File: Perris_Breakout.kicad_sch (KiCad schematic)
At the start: 21 parts, among them J1 PERRI_1, J10 SCL, J11 GND, J12 GND, J13 SDA, J14 SDA, J2 PERRI_2, J3 PERRI_3, J4 PERRI_4, J5 PERRI_5, J6 PERRI_6, J7 PERRI_7, J8 PERRI_8, J9 SCL

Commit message: Changed copper zone properties
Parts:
- J1, J2, J3, J4, J5, J6, J7, J8: footprint Connector_PinHeader_2.54mm:PinHeader_2x05_P2.54mm_Vertical -> HELIX:Perri_conn_2x5_Reverse
- J10, J9, TP1: value SCL -> SDA
- J13, J14, TP3: value SDA -> SCL
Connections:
- net SCL: now also J13.1 (Pin_1), J14.1 (Pin_1), TP3.1; no longer J10.1 (Pin_1), J9.1 (Pin_1), TP1.1
- net SDA: now also J10.1 (Pin_1), J9.1 (Pin_1), TP1.1; no longer J13.1 (Pin_1), J14.1 (Pin_1), TP3.1
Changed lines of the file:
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@@
+    (effects (font (size 1.27 1.27)) (justify left bottom))
+  )
+  (label "SDA" (at 199.39 93.98 0)
     (effects (font (size 1.27 1.27)) (justify left bottom))
   )
@@
     (effects (font (size 1.27 1.27)) (justify left bottom))
   )
-  (label "SDA" (at 199.39 124.46 90)
-    (effects (font (size 1.27 1.27)) (justify left bottom))
-  )
   (label "SCL" (at 101.6 54.61 180)
     (effects (font (size 1.27 1.27)) (justify right bottom))
   )
-  (label "SCL" (at 199.39 93.98 90)
-    (effects (font (size 1.27 1.27)) (justify left bottom))
-  )
   (label "SDA" (at 114.3 54.61 0)
     (effects (font (size 1.27 1.27)) (justify left bottom))
@@
   )
   (label "GND" (at 213.36 64.77 0)
+    (effects (font (size 1.27 1.27)) (justify left bottom))
+  )
+  (label "SCL" (at 199.39 124.46 0)
     (effects (font (size 1.27 1.27)) (justify left bottom))
   )
@@
       (effects (font (size 1.27 1.27)) (justify left))
     )
-    (property "Value" "SCL" (id 1) (at 180.34 83.82 90)
+    (property "Value" "SDA" (id 1) (at 180.34 83.82 90)
       (effects (font (size 1.27 1.27)) (justify left))
     )
@@
     (property "Reference" "J1" (id 0) (at 77.47 19.05 0))
     (property "Value" "PERRI_1" (id 1) (at 77.47 21.59 0))
-    (property "Footprint" "Connector_PinHeader_2.54mm:PinHeader_2x05_P2.54mm_Vertical" (id 2) (at 76.2 30.48 0)
+    (property "Footprint" "HELIX:Perri_conn_2x5_Reverse" (id 2) (at 76.2 30.48 0)
       (effects (font (size 1.27 1.27)) hide)
     )
@@
       (effects (font (size 1.27 1.27)) (justify left))
     )
-    (property "Value" "SCL" (id 1) (at 200.66 88.8999 0)
+    (property "Value" "SDA" (id 1) (at 200.66 88.8999 0)
       (effects (font (size 1.27 1.27)) (justify left))
     )
@@
     (property "Reference" "J3" (id 0) (at 73.66 97.79 0))
     (property "Value" "PERRI_3" (id 1) (at 73.66 100.33 0))
-    (property "Footprint" "Connector_PinHeader_2.54mm:PinHeader_2x05_P2.54mm_Vertical" (id 2) (at 72.39 109.22 0)
+    (property "Footprint" "HELIX:Perri_conn_2x5_Reverse" (id 2) (at 72.39 109.22 0)
       (effects (font (size 1.27 1.27)) hide)
     )
@@
     (property "Reference" "J4" (id 0) (at 73.66 138.43 0))
     (property "Value" "PERRI_4" (id 1) (at 73.66 140.97 0))
-    (property "Footprint" "Connector_PinHeader_2.54mm:PinHeader_2x05_P2.54mm_Vertical" (id 2) (at 72.39 149.86 0)
+    (property "Footprint" "HELIX:Perri_conn_2x5_Reverse" (id 2) (at 72.39 149.86 0)
       (effects (font (size 1.27 1.27)) hide)
     )
@@
       (effects (font (size 1.27 1.27)) (justify left))
     )
-    (property "Value" "SDA" (id 1) (at 220.98 113.6649 90)
+    (property "Value" "SCL" (id 1) (at 220.98 113.6649 90)
       (effects (font (size 1.27 1.27)) (justify left))
     )
@@
       (effects (font (size 1.27 1.27)) (justify left))
     )
-    (property "Value" "SDA" (id 1) (at 200.66 118.1099 0)
+    (property "Value" "SCL" (id 1) (at 200.66 118.1099 0)
       (effects (font (size 1.27 1.27)) (justify left))
     )
@@
     (property "Reference" "J2" (id 0) (at 73.66 57.15 0))
     (property "Value" "PERRI_2" (id 1) (at 73.66 59.69 0))
-    (property "Footprint" "Connector_PinHeader_2.54mm:PinHeader_2x05_P2.54mm_Vertical" (id 2) (at 72.39 68.58 0)
+    (property "Footprint" "HELIX:Perri_conn_2x5_Reverse" (id 2) (at 72.39 68.58 0)
       (effects (font (size 1.27 1.27)) hide)
     )
@@
     (property "Reference" "J8" (id 0) (at 110.49 158.75 0))
     (property "Value" "PERRI_8" (id 1) (at 110.49 161.29 0))
-    (property "Footprint" "Connector_PinHeader_2.54mm:PinHeader_2x05_P2.54mm_Vertical" (id 2) (at 109.22 170.18 0)
+    (property "Footprint" "HELIX:Perri_conn_2x5_Reverse" (id 2) (at 109.22 170.18 0)
       (effects (font (size 1.27 1.27)) hide)
     )
@@
     (property "Reference" "J6" (id 0) (at 109.22 77.47 0))
     (property "Value" "PERRI_6" (id 1) (at 109.22 80.01 0))
-    (property "Footprint" "Connector_PinHeader_2.54mm:PinHeader_2x05_P2.54mm_Vertical" (id 2) (at 107.95 88.9 0)
+    (property "Footprint" "HELIX:Perri_conn_2x5_Reverse" (id 2) (at 107.95 88.9 0)
       (effects (font (size 1.27 1.27)) hide)
     )
@@
       (effects (font (size 1.27 1.27)) (justify left))
     )
-    (property "Value" "SDA" (id 1) (at 187.96 114.3 90)
+    (property "Value" "SCL" (id 1) (at 187.96 114.3 90)
       (effects (font (size 1.27 1.27)) (justify left))
     )
@@
     (property "Reference" "J7" (id 0) (at 109.22 120.65 0))
     (property "Value" "PERRI_7" (id 1) (at 109.22 123.19 0))
-    (property "Footprint" "Connector_PinHeader_2.54mm:PinHeader_2x05_P2.54mm_Vertical" (id 2) (at 107.95 132.08 0)
+    (property "Footprint" "HELIX:Perri_conn_2x5_Reverse" (id 2) (at 107.95 132.08 0)
       (effects (font (size 1.27 1.27)) hide)
     )
@@
       (effects (font (size 1.27 1.27)) (justify left))
     )
-    (property "Value" "SCL" (id 1) (at 220.98 84.4549 90)
+    (property "Value" "SDA" (id 1) (at 220.98 84.4549 90)
       (effects (font (size 1.27 1.27)) (justify left))
     )
@@
     (property "Reference" "J5" (id 0) (at 107.95 38.1 0))
     (property "Value" "PERRI_5" (id 1) (at 107.95 40.64 0))
-    (property "Footprint" "Connector_PinHeader_2.54mm:PinHeader_2x05_P2.54mm_Vertical" (id 2) (at 106.68 49.53 0)
+    (property "Footprint" "HELIX:Perri_conn_2x5_Reverse" (id 2) (at 106.68 49.53 0)
       (effects (font (size 1.27 1.27)) hide)
     )
@@
     )
     (path "/0f85ad9d-632b-4a0c-9660-ed86ccb952da"
-      (reference "J1") (unit 1) (value "PERRI_1") (footprint "Connector_PinHeader_2.54mm:PinHeader_2x05_P2.54mm_Vertical")
+      (reference "J1") (unit 1) (value "PERRI_1") (footprint "HELIX:Perri_conn_2x5_Reverse")
     )
     (path "/70e14a08-c866-4a02-a2ef-1cf1754dd8c3"
-      (reference "J2") (unit 1) (value "PERRI_2") (footprint "Connector_PinHeader_2.54mm:PinHeader_2x05_P2.54mm_Vertical")
+      (reference "J2") (unit 1) (value "PERRI_2") (footprint "HELIX:Perri_conn_2x5_Reverse")
     )
     (path "/26c3b9cf-85ab-4f00-84f4-4534ddaef06e"
-      (reference "J3") (unit 1) (value "PERRI_3") (footprint "Connector_PinHeader_2.54mm:PinHeader_2x05_P2.54mm_Vertical")
+      (reference "J3") (unit 1) (value "PERRI_3") (footprint "HELIX:Perri_conn_2x5_Reverse")
     )
     (path "/38531b1e-f508-4809-82fa-8689e4de43ef"
-      (reference "J4") (unit 1) (value "PERRI_4") (footprint "Connector_PinHeader_2.54mm:PinHeader_2x05_P2.54mm_Vertical")
+      (reference "J4") (unit 1) (value "PERRI_4") (footprint "HELIX:Perri_conn_2x5_Reverse")
     )
     (path "/ff662b71-adf8-4b5d-9053-5bcdb30192a2"
-      (reference "J5") (unit 1) (value "PERRI_5") (footprint "Connector_PinHeader_2.54mm:PinHeader_2x05_P2.54mm_Vertical")
+      (reference "J5") (unit 1) (value "PERRI_5") (footprint "HELIX:Perri_conn_2x5_Reverse")
     )
     (path "/aa1e270e-859c-4048-a2a0-82c3aaf8b652"
-      (reference "J6") (unit 1) (value "PERRI_6") (footprint "Connector_PinHeader_2.54mm:PinHeader_2x05_P2.54mm_Vertical")
+      (reference "J6") (unit 1) (value "PERRI_6") (footprint "HELIX:Perri_conn_2x5_Reverse")
     )
     (path "/d20b730d-c092-490c-bfa2-0ceb50a6b338"
-      (reference "J7") (unit 1) (value "PERRI_7") (footprint "Connector_PinHeader_2.54mm:PinHeader_2x05_P2.54mm_Vertical")
+      (reference "J7") (unit 1) (value "PERRI_7") (footprint "HELIX:Perri_conn_2x5_Reverse")
     )
     (path "/960e653f-ae49-49f8-90f0-d203b85e7ee9"
-      (reference "J8") (unit 1) (value "PERRI_8") (footprint "Connector_PinHeader_2.54mm:PinHeader_2x05_P2.54mm_Vertical")
+      (reference "J8") (unit 1) (value "PERRI_8") (footprint "HELIX:Perri_conn_2x5_Reverse")
     )
     (path "/01f3def0-727f-4ff4-91f6-12fdb6a71365"
-      (reference "J9") (unit 1) (value "SCL") (footprint "Connector_PinHeader_2.54mm:PinHeader_1x01_P2.54mm_Vertical")
+      (reference "J9") (unit 1) (value "SDA") (footprint "Connector_PinHeader_2.54mm:PinHeader_1x01_P2.54mm_Vertical")
     )
     (path "/f99fda44-c812-4a3a-9c29-0f7fbd064e64"
-      (reference "J10") (unit 1) (value "SCL") (footprint "Connector_PinHeader_2.54mm:PinHeader_1x01_P2.54mm_Vertical")
+      (reference "J10") (unit 1) (value "SDA") (footprint "Connector_PinHeader_2.54mm:PinHeader_1x01_P2.54mm_Vertical")
     )
     (path "/24a12225-cf2f-4e3e-b597-f90f877d89bf"
@@
     )
     (path "/af41b548-bfca-440d-9bee-d6335779e8e5"
-      (reference "J13") (unit 1) (value "SDA") (footprint "Connector_PinHeader_2.54mm:PinHeader_1x01_P2.54mm_Vertical")
+      (reference "J13") (unit 1) (value "SCL") (footprint "Connector_PinHeader_2.54mm:PinHeader_1x01_P2.54mm_Vertical")
     )
     (path "/3c5c2ab2-2def-494c-9a03-87ee7c16e836"
-      (reference "J14") (unit 1) (value "SDA") (footprint "Connector_PinHeader_2.54mm:PinHeader_1x01_P2.54mm_Vertical")
+      (reference "J14") (unit 1) (value "SCL") (footprint "Connector_PinHeader_2.54mm:PinHeader_1x01_P2.54mm_Vertical")
     )
     (path "/1a38f442-37f1-4c0d-b639-48acf70bf662"
-      (reference "TP1") (unit 1) (value "SCL") (footprint "Connector_PinHeader_2.54mm:PinHeader_1x01_P2.54mm_Vertical")
+      (reference "TP1") (unit 1) (value "SDA") (footprint "Connector_PinHeader_2.54mm:PinHeader_1x01_P2.54mm_Vertical")
     )
     (path "/3a03a9f2-3b31-49df-b740-9fe8bd6dc7ac"
@@
     )
     (path "/4f164f8e-bc3b-4e49-bbb8-c1d623c879a3"
-      (reference "TP3") (unit 1) (value "SDA") (footprint "Connector_PinHeader_2.54mm:PinHeader_1x01_P2.54mm_Vertical")
-    )
-  )
+      (reference "TP3") (unit 1) (value "SCL") (footprint "Connector_PinHeader_2.54mm:PinHeader_1x01_P2.54mm_Vertical")
+    )
+  )

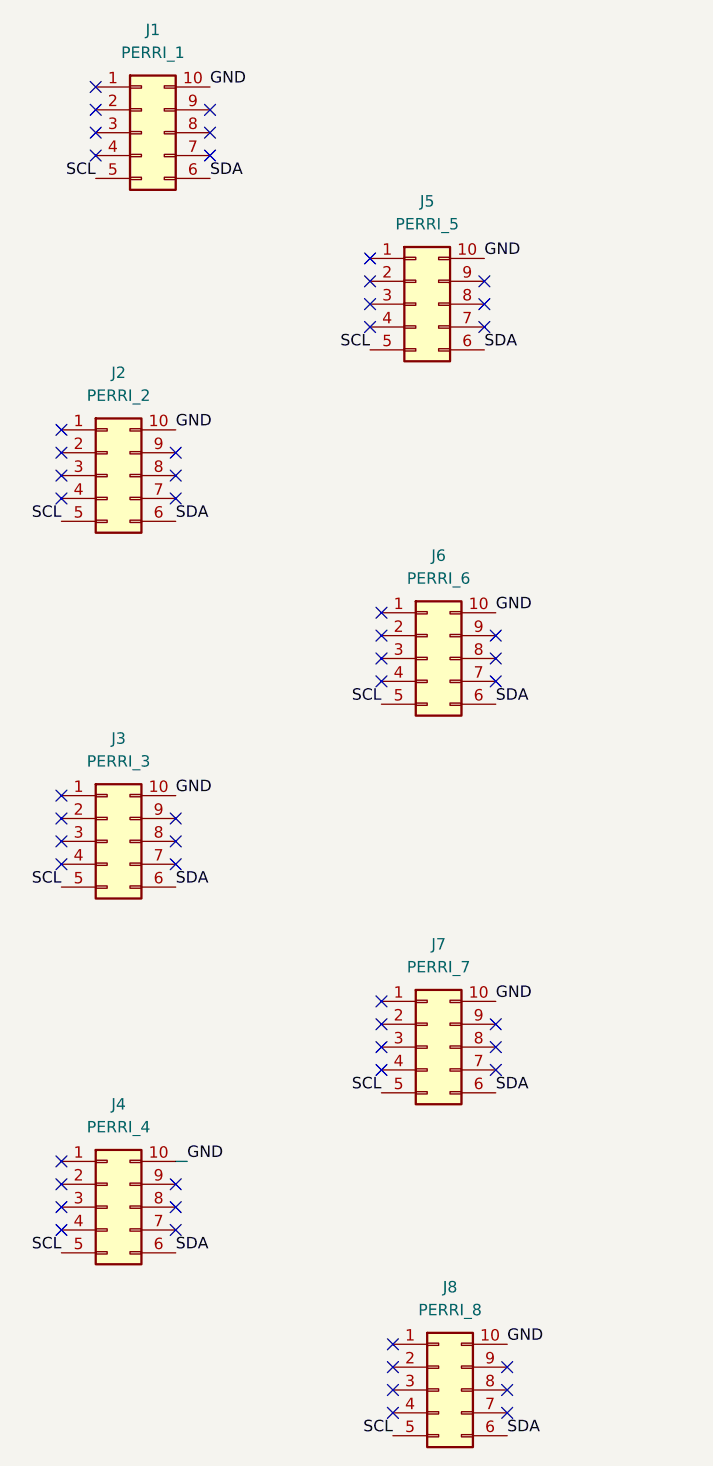
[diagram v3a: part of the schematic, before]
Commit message: Updated Schematic to add GND, SCL, SDA nets to unused pins. Upated PCB to add filled copper zones for SDA, SCL, and GND nets. Generated new drill and gerber files
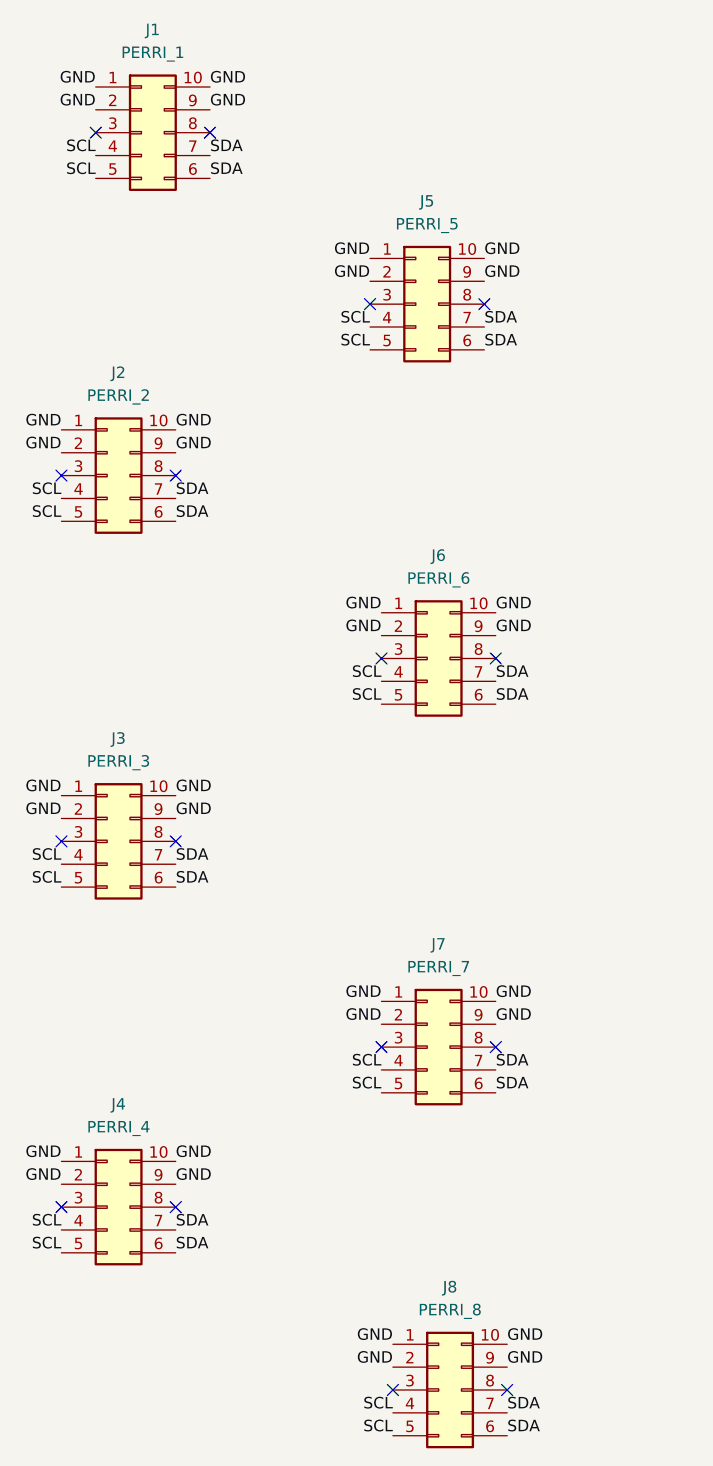
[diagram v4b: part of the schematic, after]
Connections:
- net GND: now also J1.1 (Pin_1), J1.2 (Pin_2), J1.9 (Pin_9), J2.1 (Pin_1), J2.2 (Pin_2), J2.9 (Pin_9), J3.1 (Pin_1), J3.2 (Pin_2), J3.9 (Pin_9), J4.1 (Pin_1), J4.2 (Pin_2), J4.9 (Pin_9), J5.1 (Pin_1), J5.2 (Pin_2), J5.9 (Pin_9), J6.1 (Pin_1), J6.2 (Pin_2), J6.9 (Pin_9), J7.1 (Pin_1), J7.2 (Pin_2), J7.9 (Pin_9), J8.1 (Pin_1), J8.2 (Pin_2), J8.9 (Pin_9)
- net SCL: now also J1.4 (Pin_4), J2.4 (Pin_4), J3.4 (Pin_4), J4.4 (Pin_4), J5.4 (Pin_4), J6.4 (Pin_4), J7.4 (Pin_4), J8.4 (Pin_4)
- net SDA: now also J1.7 (Pin_7), J2.7 (Pin_7), J3.7 (Pin_7), J4.7 (Pin_7), J5.7 (Pin_7), J6.7 (Pin_7), J7.7 (Pin_7), J8.7 (Pin_7)
- no-connect marks 56 -> 16
